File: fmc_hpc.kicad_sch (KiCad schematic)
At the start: 24 parts, among them J5 ASP-134486-01

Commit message: Finish routing FMC, start routing remainig misc signals
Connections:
- net FMC_IO_11_N: now also J5.K23 (HA23_N); no longer J5.J13 (HA11_N)
- net FMC_IO_11_P: now also J5.K22 (HA23_P); no longer J5.J12 (HA11_P)
- net FMC_IO_12_N: now also J5.J22 (HA22_N); no longer J5.K11 (HA06_N)
- net FMC_IO_12_P: now also J5.J21 (HA22_P); no longer J5.K10 (HA06_P)
- net FMC_IO_13_N: now also J5.K20 (HA21_N); no longer J5.J10 (HA07_N)
- net FMC_IO_13_P: now also J5.K19 (HA21_P); no longer J5.J9 (HA07_P)
- net FMC_IO_14_N: now also J5.J25 (HB01_N); no longer J5.K14 (HA10_N)
- net FMC_IO_14_P: now also J5.J24 (HB01_P); no longer J5.K13 (HA10_P)
- net FMC_IO_15_N: now also J5.J7 (HA03_N); no longer J5.K20 (HA21_N)
- net FMC_IO_15_P: now also J5.J6 (HA03_P); no longer J5.K19 (HA21_P)
- net FMC_IO_16_N: now also J5.K8 (HA02_N); no longer J5.J22 (HA22_N)
- net FMC_IO_16_P: now also J5.K7 (HA02_P); no longer J5.J21 (HA22_P)
- net FMC_IO_17_N: now also J5.K17 (HA17_N_CC); no longer J5.J7 (HA03_N)
- net FMC_IO_17_P: now also J5.K16 (HA17_P_CC); no longer J5.J6 (HA03_P)
- net FMC_IO_18_N: now also J5.J10 (HA07_N); no longer J5.K23 (HA23_N)
- net FMC_IO_18_P: now also J5.J9 (HA07_P); no longer J5.K22 (HA23_P)
- net FMC_IO_20_N: now also J5.K26 (HB00_N_CC); no longer J5.J16 (HA14_N)
- net FMC_IO_20_P: now also J5.K25 (HB00_P_CC); no longer J5.J15 (HA14_P)
- net FMC_IO_21_N: now also J5.K11 (HA06_N); no longer J5.J25 (HB01_N)
- net FMC_IO_21_P: now also J5.K10 (HA06_P); no longer J5.J24 (HB01_P)
- net FMC_IO_23_N: now also J5.J13 (HA11_N); no longer J5.K26 (HB00_N_CC)
- net FMC_IO_23_P: now also J5.J12 (HA11_P); no longer J5.K25 (HB00_P_CC)
- net FMC_IO_24_N: now also J5.J28 (HB07_N); no longer J5.K17 (HA17_N_CC)
- net FMC_IO_24_P: now also J5.J27 (HB07_P); no longer J5.K16 (HA17_P_CC)
- net FMC_IO_25: now also J5.K28 (HB06_P_CC); no longer J5.J18 (HA18_P)
- net FMC_IO_5_N: now also J5.J19 (HA18_N); no longer J5.K8 (HA02_N)
- net FMC_IO_5_P: now also J5.J18 (HA18_P); no longer J5.K7 (HA02_P)
- net VIN: no longer C257.1, C258.1
- net 12P0V: now reaches D18.A, J5.C35 (12P0V), J5.C37 (12P0V)
- net 12P0V: now also C257.1, C258.1
- no-connect marks 24 -> 27
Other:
- moved on the sheet: C257, C258, C259, C260, C261, C262, C263, C264, C265, C266, C267, C268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

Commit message: Cleanup schematic
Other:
- note added: "FMC HPC"
- moved on the sheet: C257, C258, C259, C260, C261, C262, C263, C264, C265, C266, C267, C268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

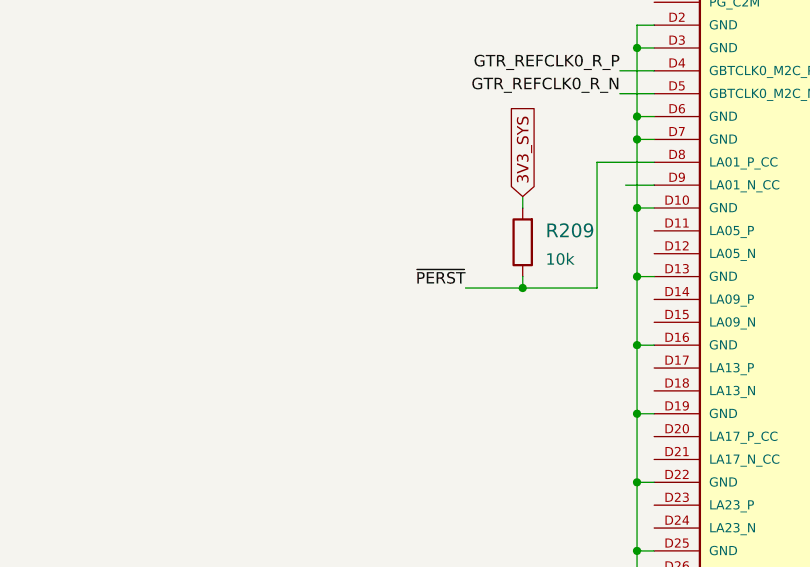
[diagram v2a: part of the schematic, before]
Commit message: Assign and connect misc. signals. Add, place and route decoupling capacitors
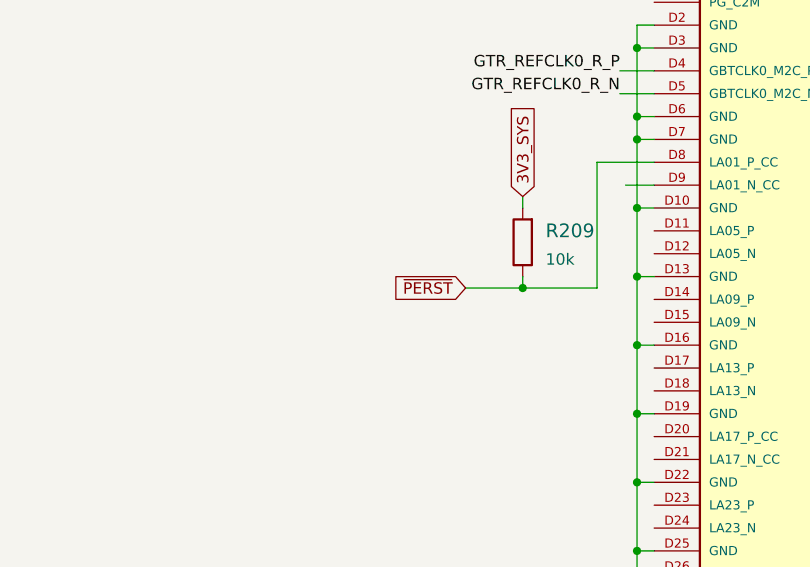
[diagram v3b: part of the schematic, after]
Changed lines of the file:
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@@
     (effects (font (size 1.27 1.27)) (justify left bottom))
-  )
-  (label "~{PERST}" (at 172.339 205.613 180)
-    (effects (font (size 1.27 1.27)) (justify right bottom))
   )
   (label "GTX_TX2_C_N" (at 324.485 99.06 0)
@@
     )
   )
+  (global_label "~{PERST}" (shape input) (at 172.339 205.613 180) (fields_autoplaced)
+    (effects (font (size 1.27 1.27)) (justify right))
+    (property "Intersheet References" "${INTERSHEET_REFS}" (id 0) (at 164.1486 205.5336 0)
+      (effects (font (size 1.27 1.27)) (justify right) hide)
+    )
+  )

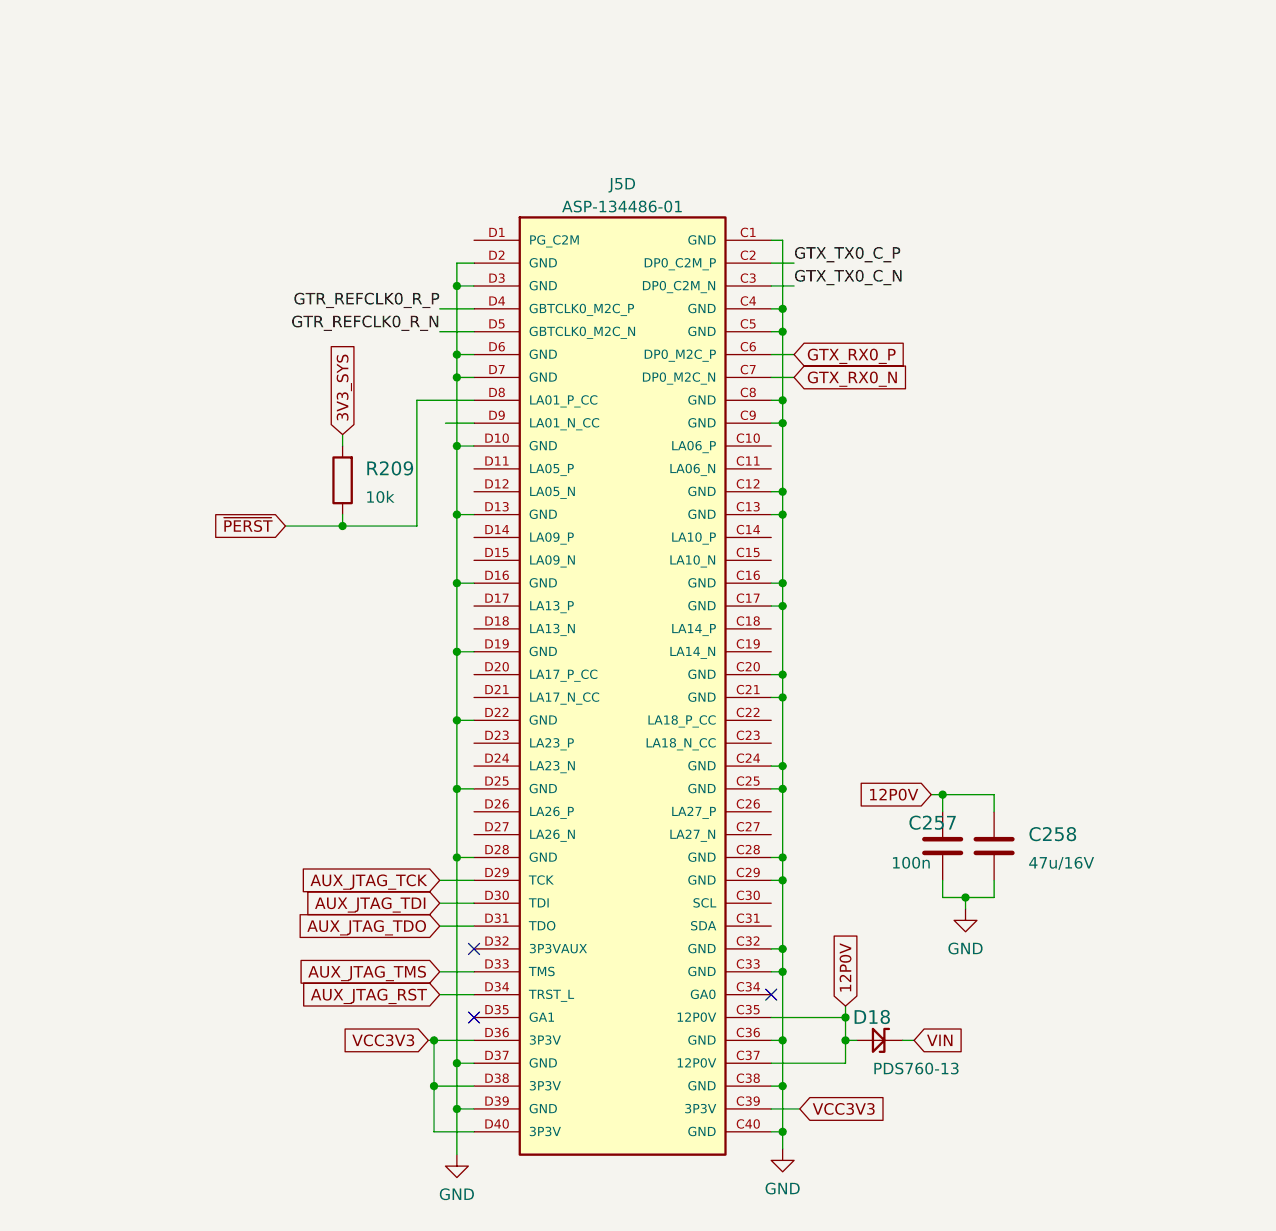
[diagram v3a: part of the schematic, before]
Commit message: Finish power supply polygons, improve connector shield to ground connection
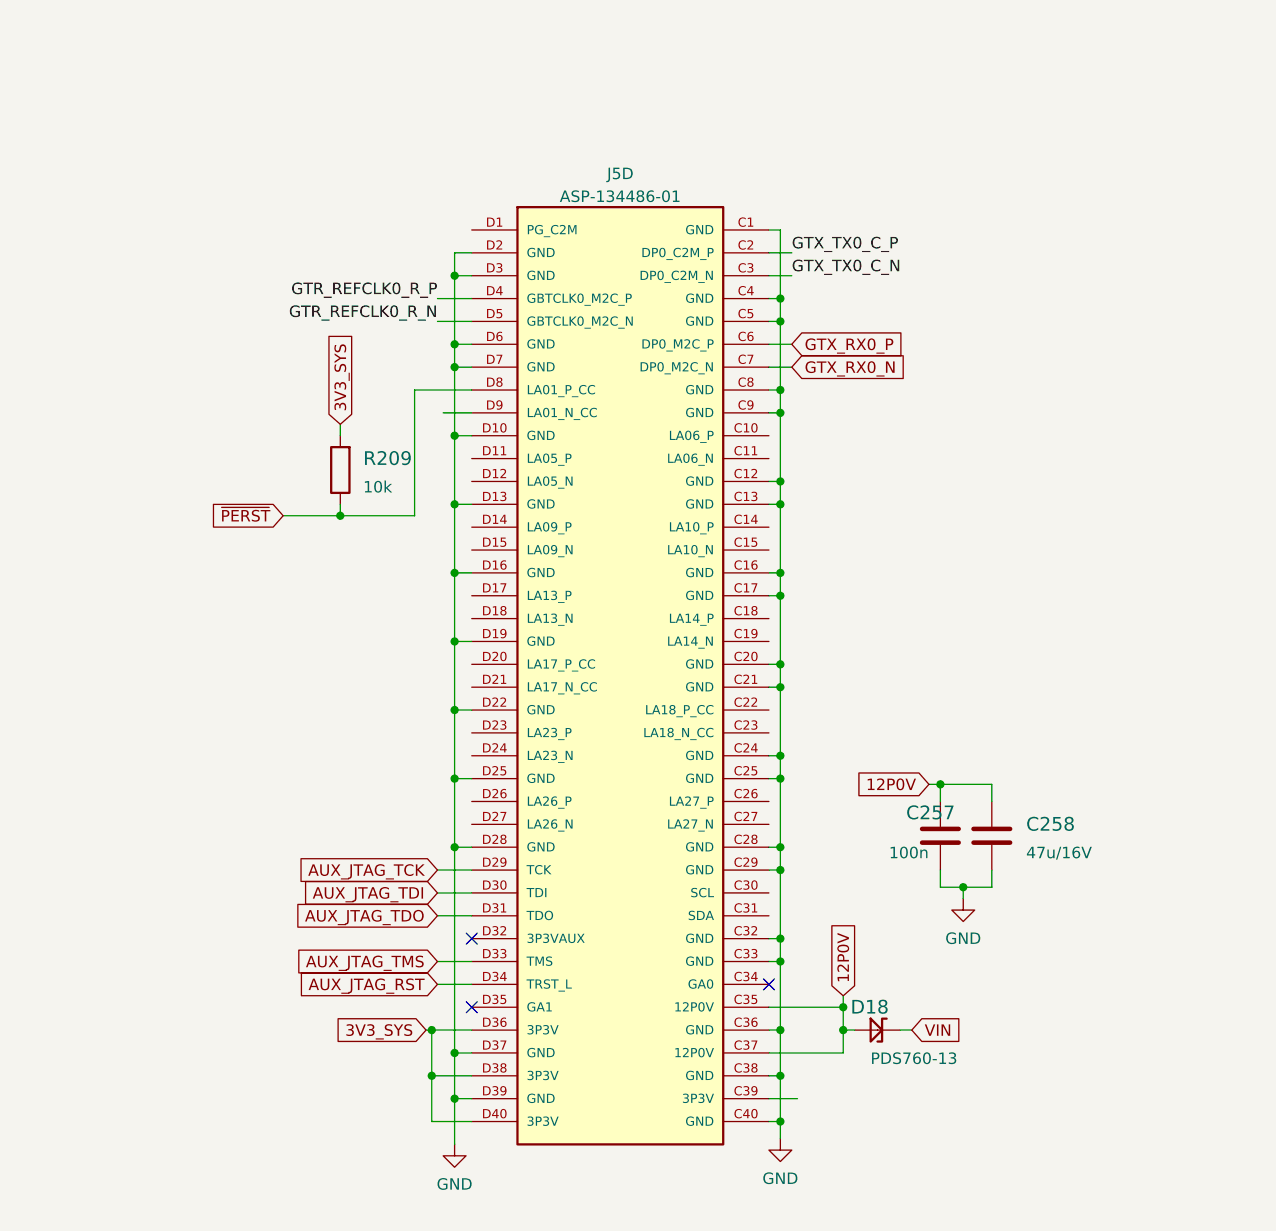
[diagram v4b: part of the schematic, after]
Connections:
- net 3V3_SYS: now also J5.D36 (3P3V), J5.D38 (3P3V), J5.D40 (3P3V)
- removed net VCC3V3: J5.C39 (3P3V), J5.D36 (3P3V), J5.D38 (3P3V), J5.D40 (3P3V)
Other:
- moved on the sheet: C257, C258, D18, J5D, R209

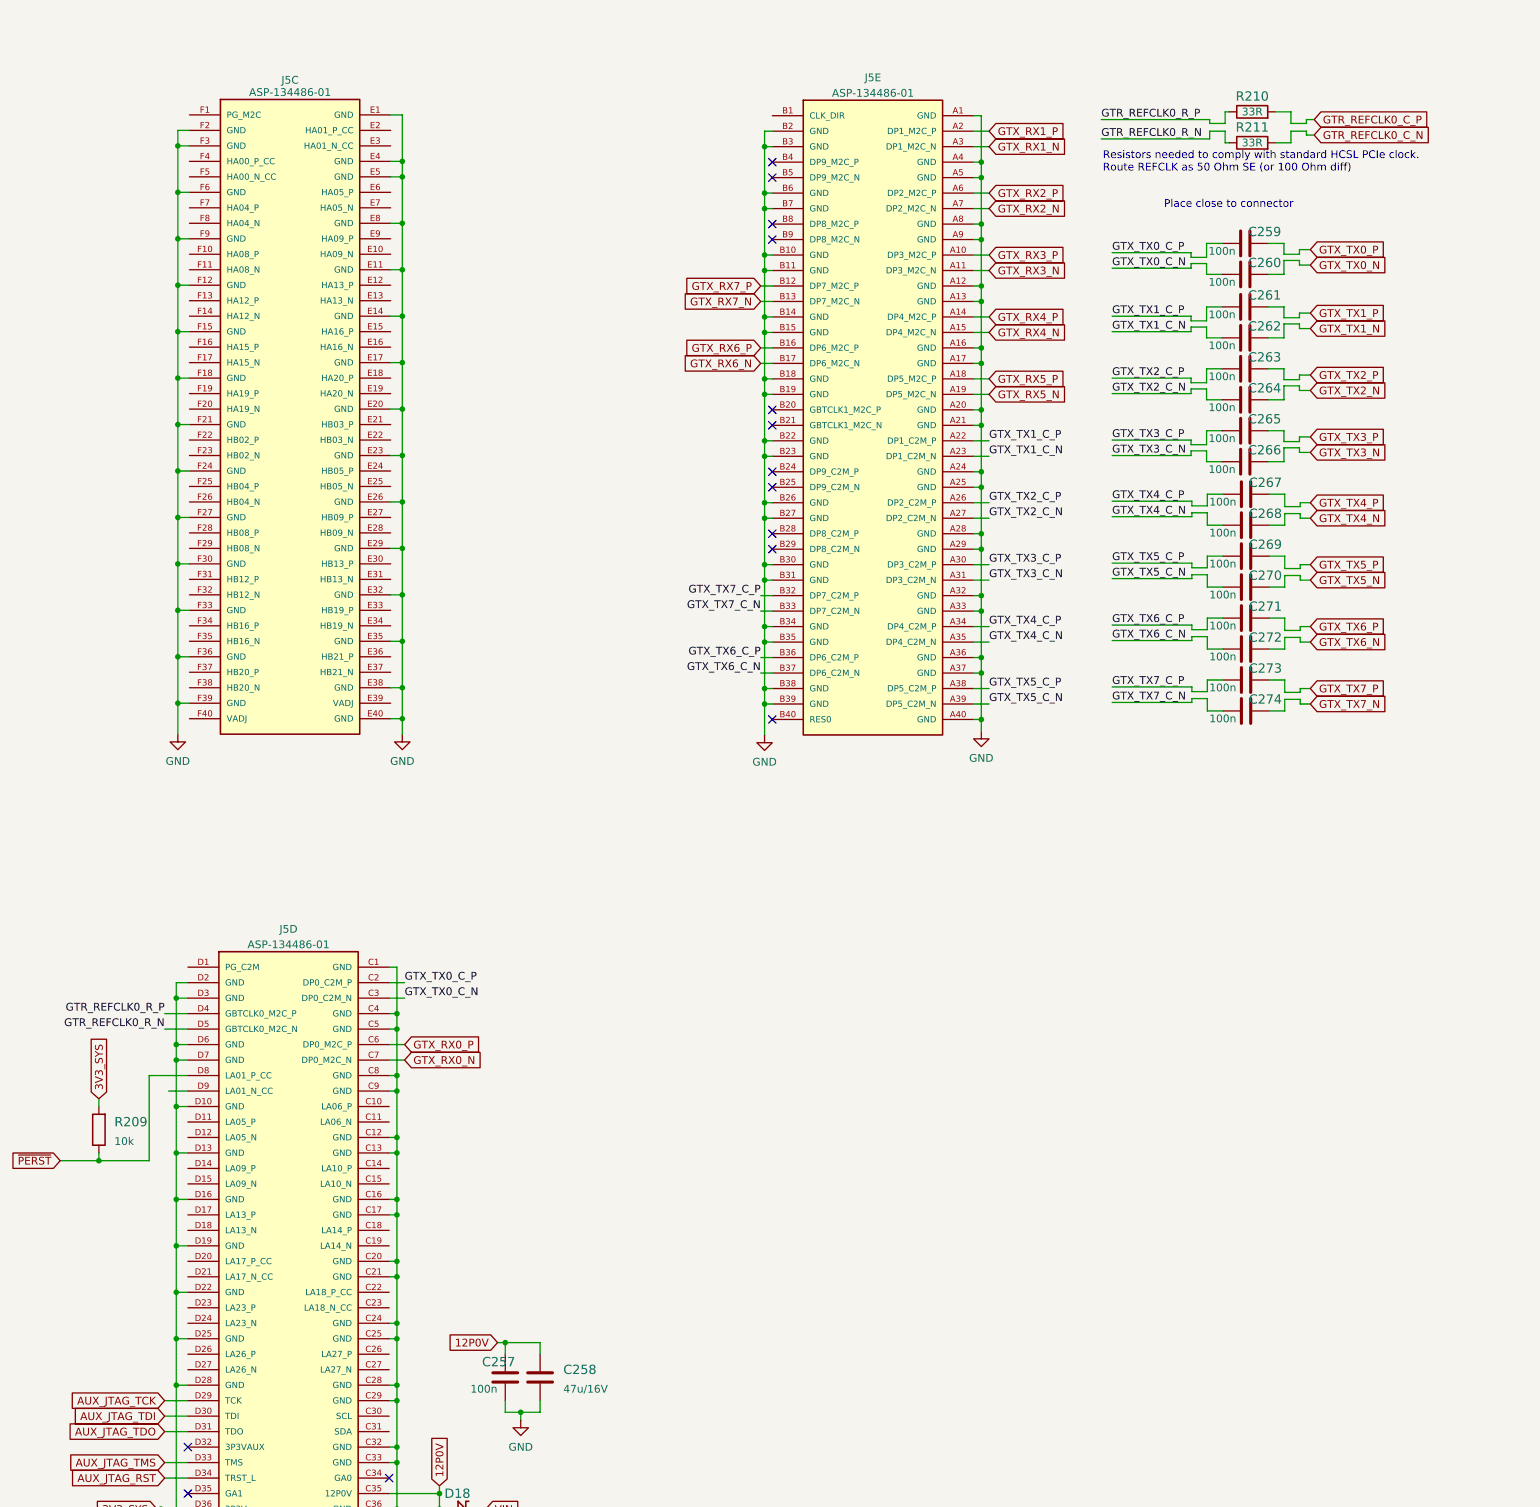
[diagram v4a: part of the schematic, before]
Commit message: Readability improvements
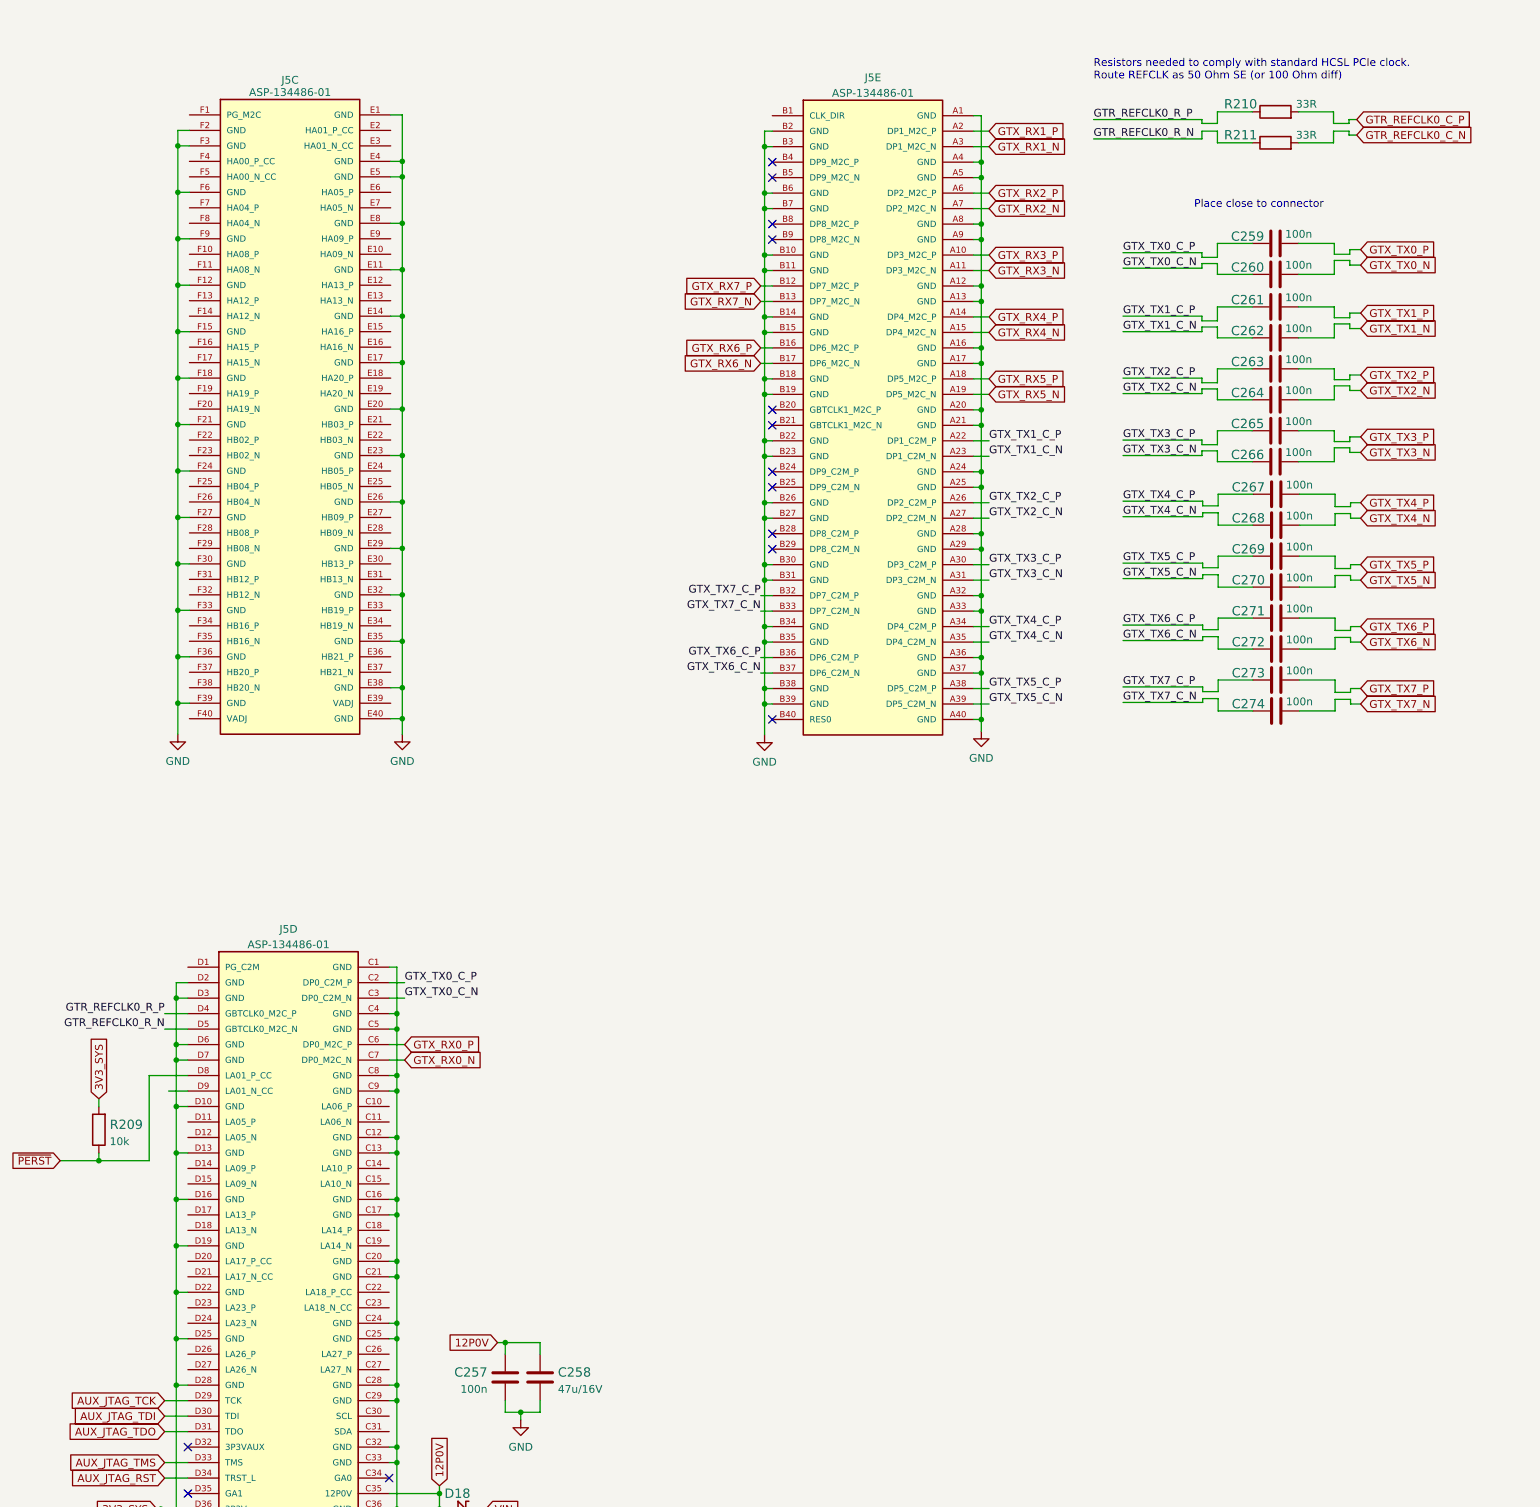
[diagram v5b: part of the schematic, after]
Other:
- moved on the sheet: C259, C260, C261, C262, C263, C264, C265, C266, C267, C268, C269, C270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

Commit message: Optimize BOM, add all bank 115 and 116 REFCLK's to FMC connector
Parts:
- added R148, R149, R150, R151, R152, R153: R_33R_0402, antmicro-footprints:0402-res, symbol antmicroResistors0402:R_33R_0402
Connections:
- net GTR_REFCLK1_R_P: now reaches J5.B20 (GBTCLK1_M2C_P)
- net GTR_REFCLK1_R_P: now also R148.1
- net GTR_REFCLK1_R_N: now reaches J5.B21 (GBTCLK1_M2C_N)
- net GTR_REFCLK1_R_N: now also R149.1
- net GTR_REFCLK3_R_P: now reaches J5.J2 (CLK3_BIDIR_P)
- net GTR_REFCLK3_R_P: now also R152.1
- net GTR_REFCLK3_R_N: now reaches J5.J3 (CLK3_BIDIR_N)
- net GTR_REFCLK3_R_N: now also R153.1
- net GTR_REFCLK2_R_P: now reaches J5.K4 (CLK2_BIDIR_P)
- net GTR_REFCLK2_R_P: now also R150.1
- net GTR_REFCLK2_R_N: now reaches J5.K5 (CLK2_BIDIR_N)
- net GTR_REFCLK2_R_N: now also R151.1
- net FMC_IO_15_N: no longer names the net of J5.J7 (HA03_N)
- net FMC_IO_15_P: no longer names the net of J5.J6 (HA03_P)
- net FMC_IO_22_N: no longer names the net of J5.H32 (LA28_N)
- net FMC_IO_22_P: no longer names the net of J5.H31 (LA28_P)
- new net GTR_REFCLK1_C_N: R149.2
- new net GTR_REFCLK1_C_P: R148.2
- new net GTR_REFCLK2_C_N: R151.2
- new net GTR_REFCLK2_C_P: R150.2
- new net GTR_REFCLK3_C_N: R153.2
- new net GTR_REFCLK3_C_P: R152.2
- no-connect marks 27 -> 25
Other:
- moved on the sheet: C259, C260, C261, C262, C263, C264, C265, C266, C267, C268, C269, C270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
